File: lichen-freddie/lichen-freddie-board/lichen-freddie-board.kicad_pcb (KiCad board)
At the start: 2 copper layers, 139.4 x 108 mm, 37 parts, among them J1 3.5mm_Stereo, J2 Eurorack_Power

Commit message: v1.1 of Freddie and Bifocals hardware.
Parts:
- added MH1: MountingHole_2.2mm_M2, MountingHole:MountingHole_2.2mm_M2, F.Cu at (120.0, 212.6)
- added MH2: MountingHole_2.2mm_M2, MountingHole:MountingHole_2.2mm_M2, F.Cu at (170.9, 212.6)
- added MH3: MountingHole_2.2mm_M2, MountingHole:MountingHole_2.2mm_M2, F.Cu at (221.9, 212.6)
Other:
- board text added: "Lichen Community Systems Freddie v1.1 Copyright 2024 Colin Clark"
- board text removed: "Lichen Community Systems Freddie v1.0 Copyright 2024 Colin Clark"

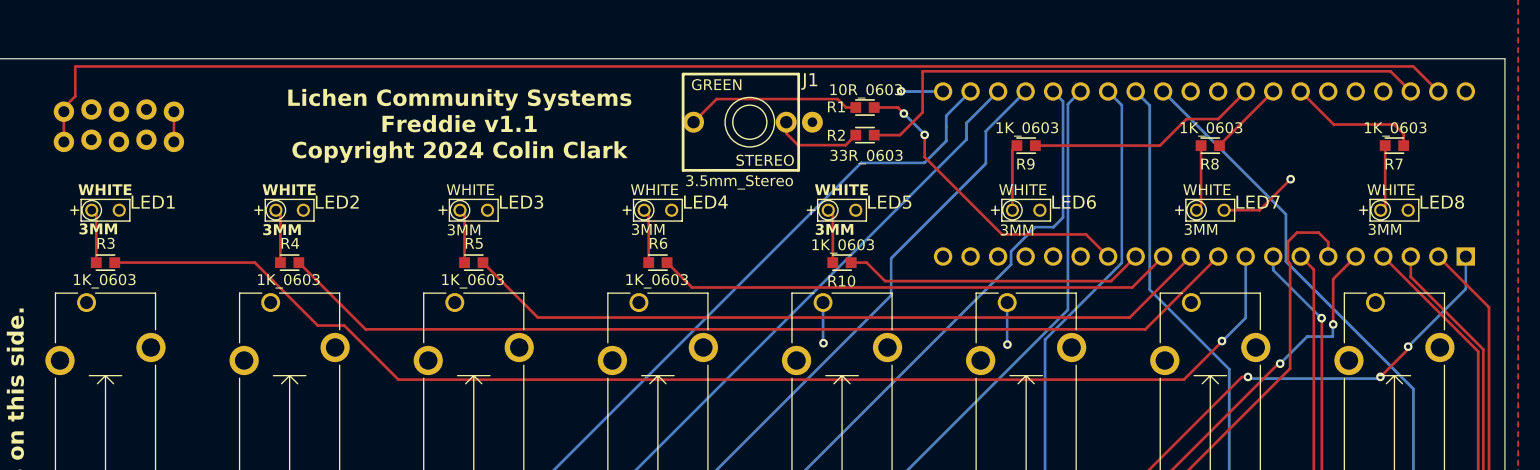
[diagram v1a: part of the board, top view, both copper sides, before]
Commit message: Updates Lichen component library and most module prototypes.
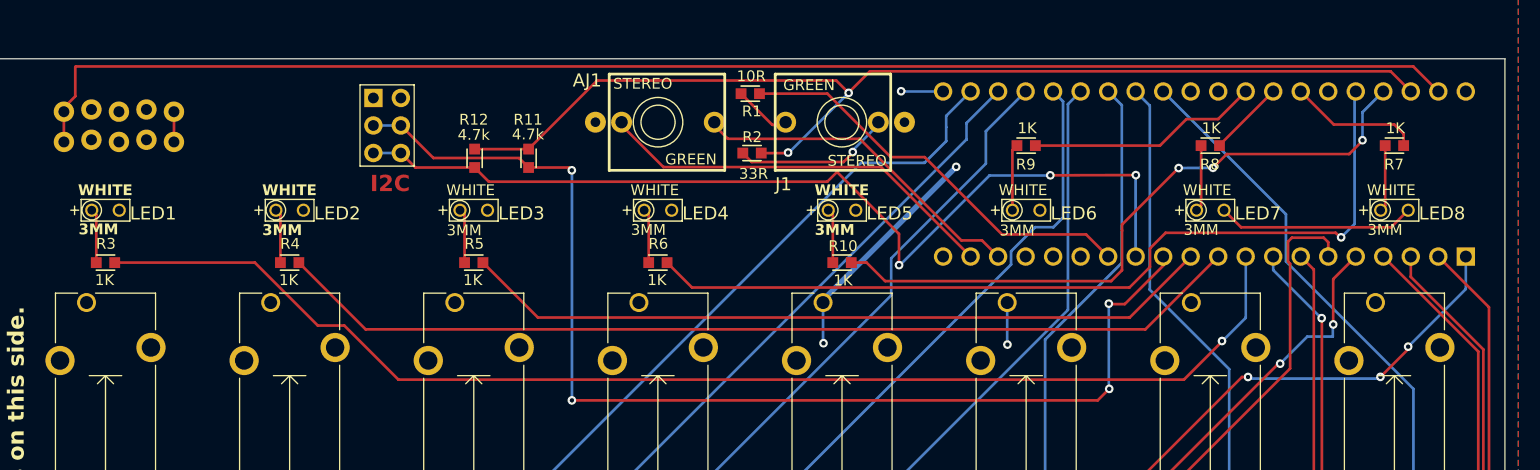
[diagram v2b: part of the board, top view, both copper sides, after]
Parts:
- added AJ1: 3.5mm_Stereo, PCM_4ms_Jack:EighthInch_Stereo_PJ366ST, F.Cu at (162.4, 116.1)
- added H2: Conn_02x03, PCM_4ms_Connector:Pins_2x03_2.54mm_TH, F.Cu at (137.4, 116.4)
- added R11: 4.7k, PCM_4ms_Resistor:R_0603, F.Cu at (150.5, 119.4)
- added R12: 4.7k, PCM_4ms_Resistor:R_0603, F.Cu at (145.5, 119.4)
- R1: value 10R_0603 -> 10R
- R10, R3, R4, R5, R6, R7, R8, R9: value 1K_0603 -> 1K
- R2: value 33R_0603 -> 33R
- moved R1 10.7 mm to (171.0, 113.5)
- moved R2 10.6 mm to (171.1, 119.0)
- moved J1 8.50 mm to (179.4, 116.1)
- renumbered J2 to H1
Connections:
- net Net-(A1-3V3_D) renamed 3V3D
- A1 pad 12: LED_GPIO_4 -> I2C_SCL
- A1 pad 13: LED_GPIO_5 -> I2C_SDA
- A1 pad 18: unconnected-(A1-AUDIO_OUT_1-Pad18) -> Net-(A1-AUDIO_OUT_1)
- A1 pad 19: unconnected-(A1-AUDIO_OUT_2-Pad19) -> Net-(A1-AUDIO_OUT_2)
- A1 pad 36: unconnected-(A1-USB_D_--Pad36) -> LED_GPIO_4
- A1 pad 37: unconnected-(A1-USB_D_+-Pad37) -> LED_GPIO_5
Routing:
- net I2C_SCL: track 0.00 -> 106.8 mm, vias 0 -> 4
- net I2C_SDA: track 0.00 -> 88.2 mm, vias 0 -> 3
- net 3V3D: track 55.0 -> 101.6 mm, vias 0 -> 2
- net Net-(A1-AUDIO_OUT_2): track 0.00 -> 37.2 mm
- net LED_GPIO_5: track 27.9 -> 61.3 mm, vias 0 -> 3
- net LED_GPIO_4: track 47.9 -> 80.6 mm, vias 0 -> 1
- net Net-(A1-AUDIO_OUT_1): track 0.00 -> 31.2 mm
- net +3.3VA: track 11.6 -> 29.2 mm, vias 3 -> 4
- net GND: track 7.34 -> 18.3 mm, vias 1 -> 0
- net Net-(J1-SIG): track 16.2 -> 5.31 mm
- net USART_TX: track 28.9 -> 38.8 mm, vias 2 -> 0
- net Net-(J1-SW): track 8.28 -> 14.6 mm, vias 0 -> 1
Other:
- board text added: "GND"
- board text added: "I2C"
- board text added: "SCL"
- board text added: "SDA"
